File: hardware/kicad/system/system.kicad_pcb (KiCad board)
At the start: 2 copper layers, 203 x 133 mm, 131 parts, among them M501 IRF530, Q201 IRF540N, Q202 IRF530, Q401 IRF530, SW201 Switch, U201 LM7805, U202 MCP601, U203 NE555, U204 ILD74, U205 MCP601, U206 IR2110, U207 4N25, U208 IR2110, U301 MCP601, U302 IL300, U303 MCP601, U401 CNY17, U402 IR2110, U501 CNY17, U502 IR2110

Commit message: system PCB: scripted placement recovery (auto-floorplan)
Rebuild the integrated-board placement after an unsaved-work loss, via
tools/place_system.py (pcbnew): edge connectors on the borders, the 5 board
clusters shelf-packed into their regions (big parts first), test-point row
along the bottom, R_STAR on the GND/GND_MCU boundary, Edge.Cuts 200x130 mm
(<=203.2 wide for the SRM-20). All 131 footprints on-board, non-overlapping.
First-pass auto-placement; fine-tune by hand from here.
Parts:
- moved U301 336.7 mm to (23.5, 105.5)
- moved R302 336.4 mm to (23.1, 118.7)
- moved U302 335.2 mm to (36.5, 105.5)
- moved U303 333.7 mm to (49.6, 105.5)
- moved R305 323.0 mm to (35.3, 118.7)
- moved R301 312.6 mm to (47.6, 118.7)
- moved Q401 312.4 mm to (111.7, 75.0)
- moved R403 311.4 mm to (99.1, 83.8)
- moved C404 309.7 mm to (100.7, 75.8)
- moved D403 300.2 mm to (123.0, 83.6)
- moved R401 297.1 mm to (111.0, 83.8)
- moved U402 296.9 mm to (136.7, 25.6)
- moved R303 295.7 mm to (62.3, 105.5)
- moved R402 293.4 mm to (122.8, 73.1)
- moved L401 290.6 mm to (101.4, 41.3)
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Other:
- board size 203 x 133 mm -> 200 x 130 mm

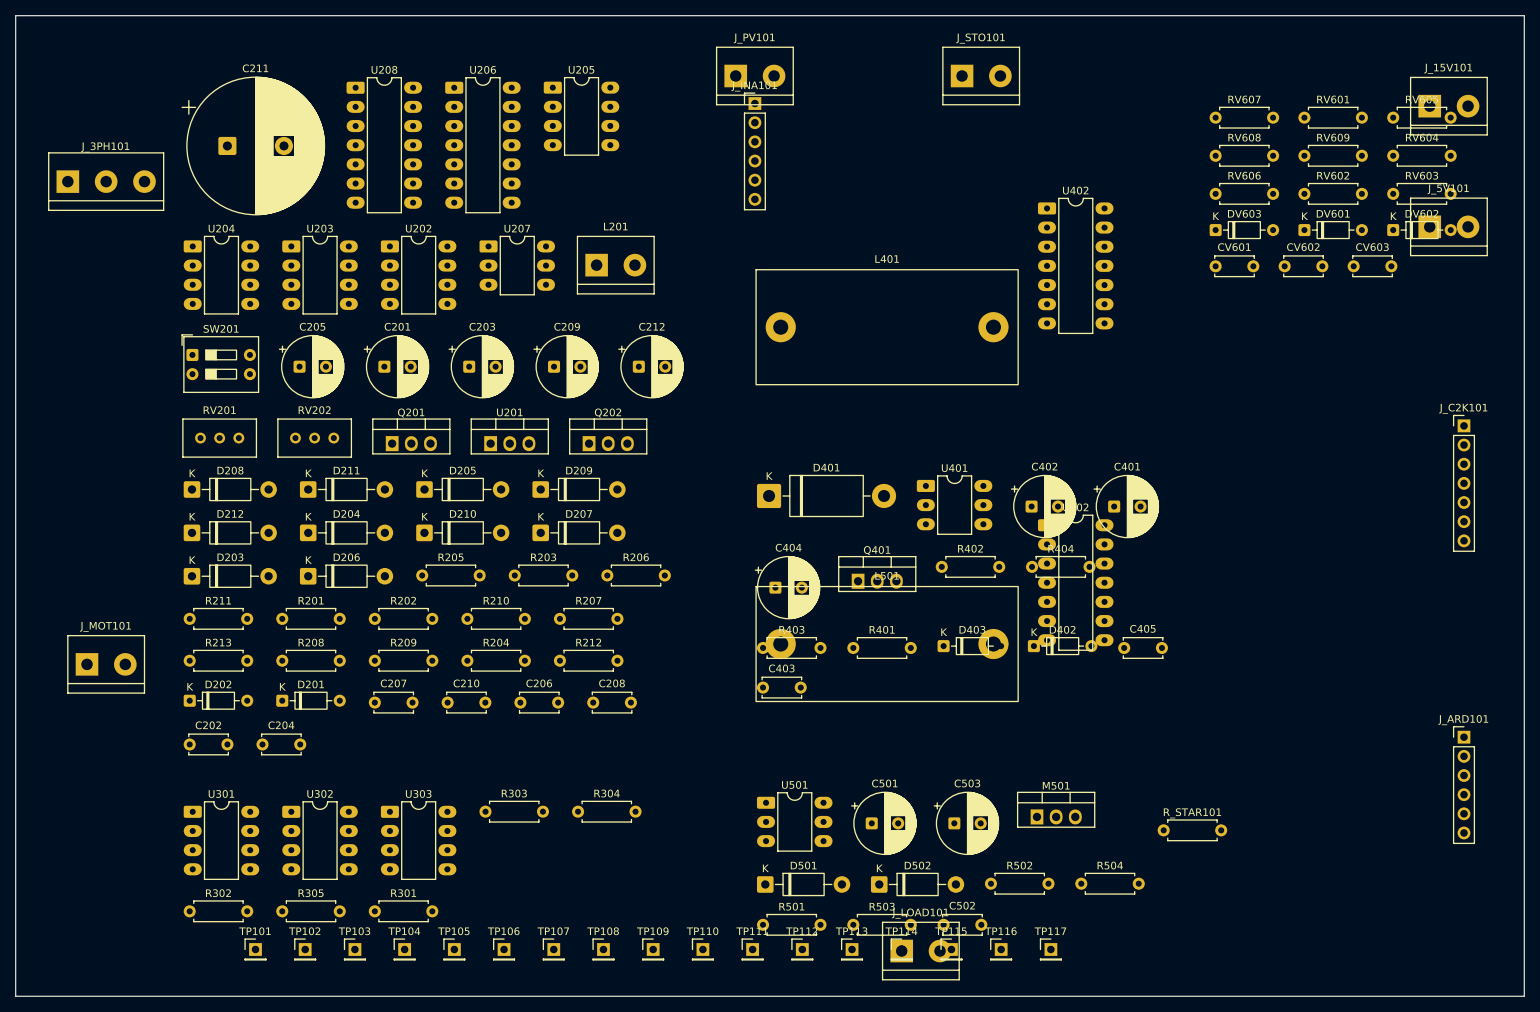
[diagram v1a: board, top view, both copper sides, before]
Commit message: system PCB: repack placement — 0 overlaps, toroids fixed, clusters clear
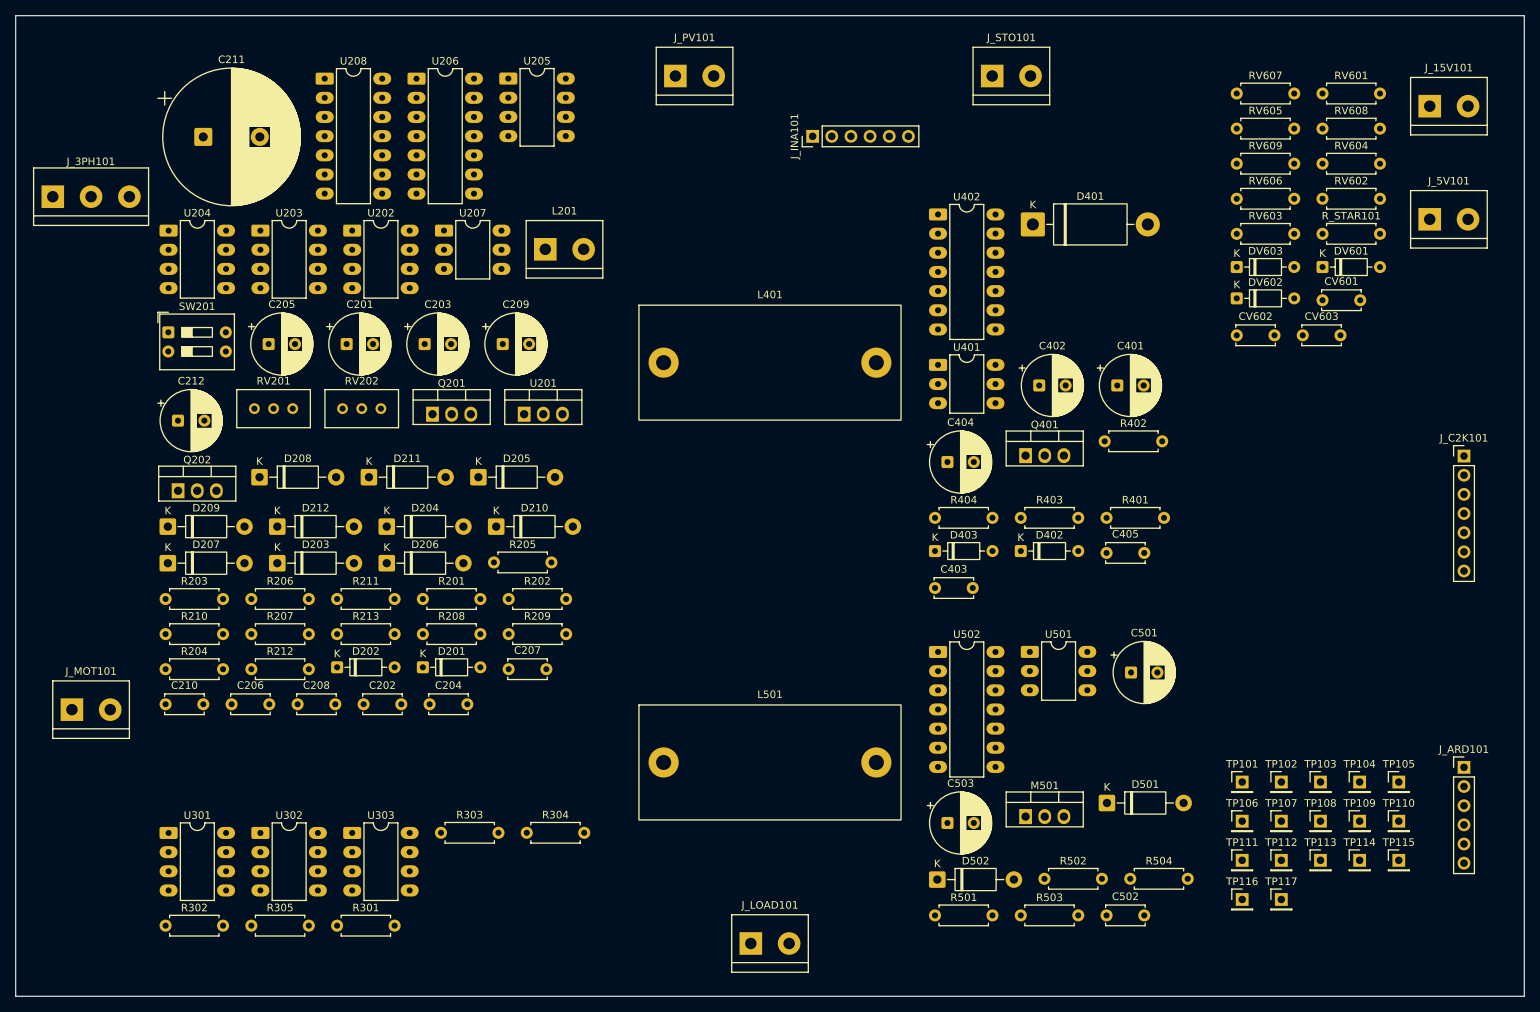
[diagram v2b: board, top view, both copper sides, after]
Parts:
- moved TP101 132.7 mm to (162.6, 101.6)
- moved TP102 131.3 mm to (167.8, 101.6)
- moved TP103 129.9 mm to (173.0, 101.6)
- moved TP104 128.5 mm to (178.2, 101.6)
- moved TP105 127.2 mm to (183.4, 101.6)
- moved TP106 99.3 mm to (162.6, 106.8)
- moved TP107 97.9 mm to (167.8, 106.8)
- moved TP108 96.6 mm to (173.0, 106.8)
- moved TP109 95.2 mm to (178.2, 106.8)
- moved TP110 93.8 mm to (183.4, 106.8)
- moved R_STAR101 81.8 mm to (173.2, 28.9)
- moved TP111 66.0 mm to (162.6, 112.0)
- moved TP112 64.6 mm to (167.8, 112.0)
- moved TP113 63.2 mm to (173.0, 112.0)
- moved TP114 61.8 mm to (178.2, 112.0)
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
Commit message: system PCB: routing prep (track 1.0, GND pour both layers) + board/CAM updates
system board:
- fix Default netclass track 0.9 -> 1.0 mm (was below min_track_width, every
  trace would have failed DRC); clearance 1.0, via 2.4/1.0 in .kicad_pro + board
- pour GND on F.Cu and B.Cu (edge inset 0.5 mm, solid pad tie)
- routing tooling: route_prep (netclass+pour), export_dsn_noplane (route GND as
  tracks; Freerouting 1.9.0 chokes on full-board planes), route_finish (SES
  import + refill + sparse GND stitching), inspect_system

srm-cam: bump submodule to double-sided support (90 rotation, bottom-side bed
leveling, GUI ruler/STOP/probe-grid, run-time estimator)

production: rename boost_v2_mill nc -> board_*, add drive_circuit trace rework
boards: buck_v2, current_sense, c2000_feedback edits; BOM + AD3 lab-guide
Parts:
- moved J_5V101 126.8 mm to (290.6, 100.7), turned to 90 degrees
- moved J_LOAD101 126.2 mm to (198.0, 199.2), turned to 180 degrees
- moved J_15V101 124.3 mm to (290.5, 81.6), turned to -90 degrees
- moved J_3PH101 122.0 mm to (99.1, 101.6), turned to 90 degrees
- moved J_PV101 119.8 mm to (185.4, 77.0)
- moved C209 119.6 mm to (159.2, 116.7)
- moved C203 119.6 mm to (148.9, 116.7)
- moved C401 119.6 mm to (240.7, 122.2)
- moved C201 119.6 mm to (138.5, 116.7)
- moved C402 119.6 mm to (230.3, 122.2)
- moved M501 119.6 mm to (228.5, 179.4)
- moved Q401 119.6 mm to (228.5, 131.5)
- moved C501 119.6 mm to (242.5, 160.3)
- moved C205 119.6 mm to (128.2, 116.7)
- moved R402 119.6 mm to (239.0, 129.6)
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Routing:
- net +5V_PWR: track 0.00 -> 553.1 mm, vias 0 -> 2
- net GND_MCU: track 0.00 -> 334.7 mm, vias 0 -> 4
- net +15V2: track 0.00 -> 313.8 mm, vias 0 -> 3
- net V1: track 0.00 -> 309.6 mm, vias 0 -> 2
- net +15V_GATE: track 0.00 -> 285.4 mm
- net PV_SDA: track 0.00 -> 256.6 mm, vias 0 -> 1
- net STORE: track 0.00 -> 252.2 mm
- net PWM_MOTOR: track 0.00 -> 220.0 mm, vias 0 -> 1
- net 3PH_W: track 0.00 -> 216.7 mm, vias 0 -> 4
- net 3PH_U: track 0.00 -> 193.7 mm, vias 0 -> 3
- net PV_SCL: track 0.00 -> 178.8 mm, vias 0 -> 3
- net Net-(U203-THRES): track 0.00 -> 175.0 mm, vias 0 -> 4
- net LOAD: track 0.00 -> 166.8 mm, vias 0 -> 1
- net MCU_V1: track 0.00 -> 165.7 mm
- net ADC_V1: track 0.00 -> 161.6 mm
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- added copper zone on B.Cu, net GND
- added copper zone on F.Cu, net GND

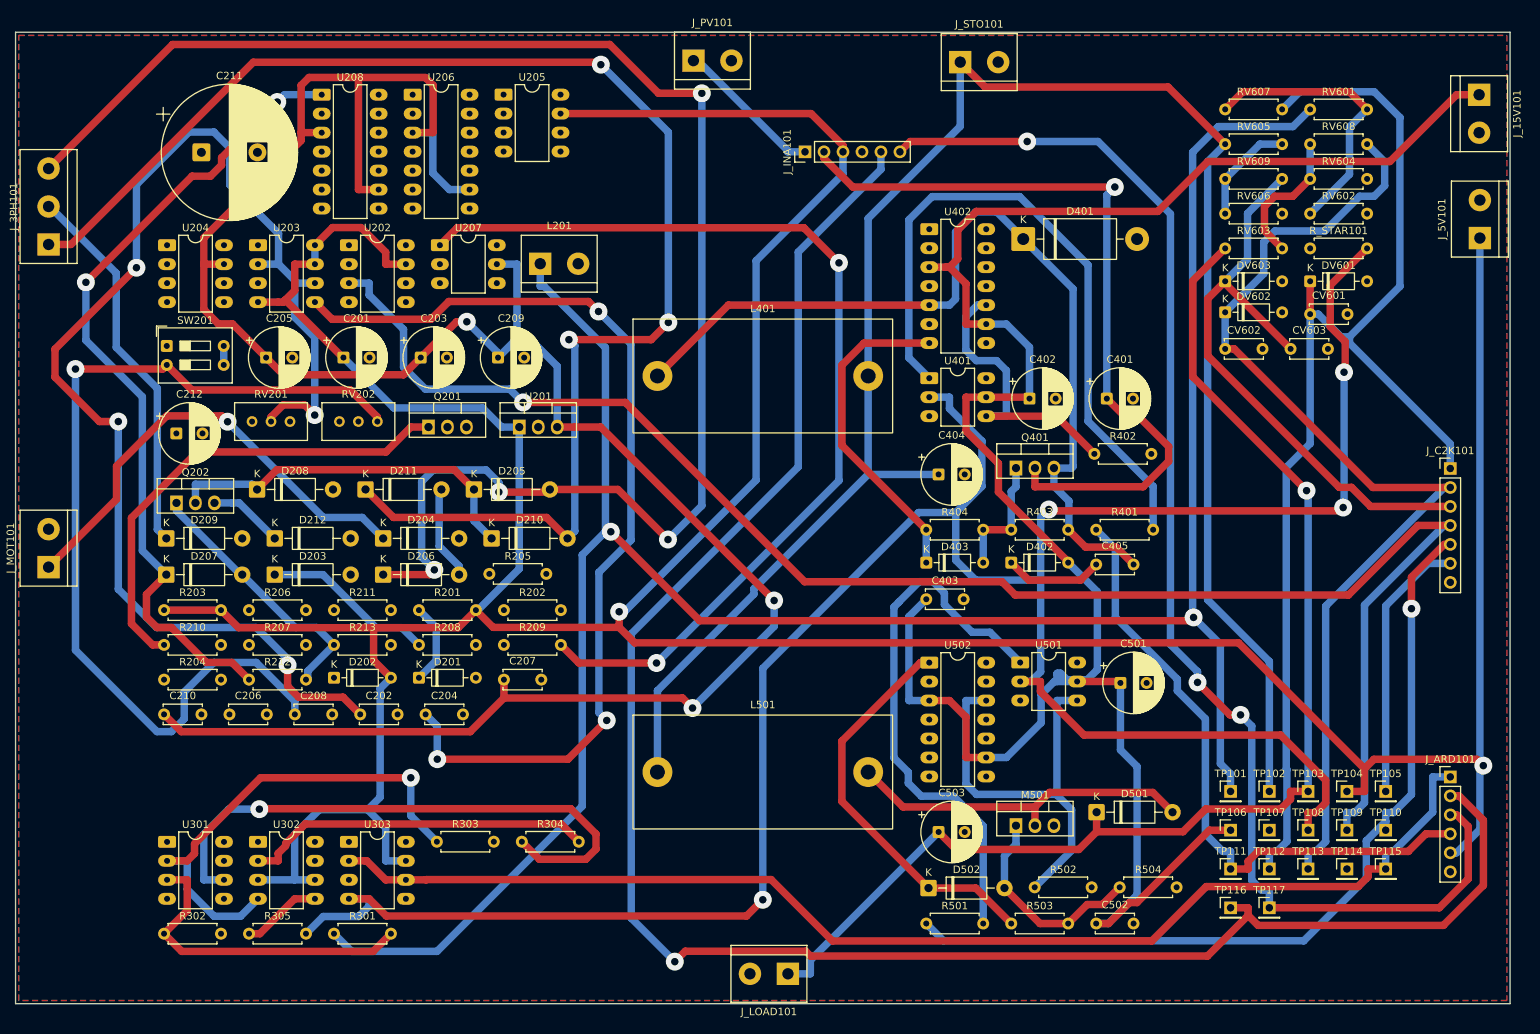
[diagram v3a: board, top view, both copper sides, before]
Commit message: system PCB: route both layers (Freerouting), DRC-clean, millable
- 1199 tracks + 67 vias (61 signal from the router + 6 GND stitches); every
  real net routed at 1.0 mm clearance, GND poured both layers
- custom DRU: pad-to-pad floor 0.8 mm (fixed 2.54 mm THT pitch can't reach the
  1.0 mm routed-copper rule) -> DRC clearance violations 246 -> 0
- gerber2rml preflight: 0.4 mm bit 0 un-millable gaps; 0.8 mm bit only 2 (0.38 mm2)
- remaining DRC: 4 silk-over-edge (cosmetic) + 24 netless NC/unused pins (benign)
- system_routed.pdf: F.Cu/B.Cu/Edge.Cuts for review
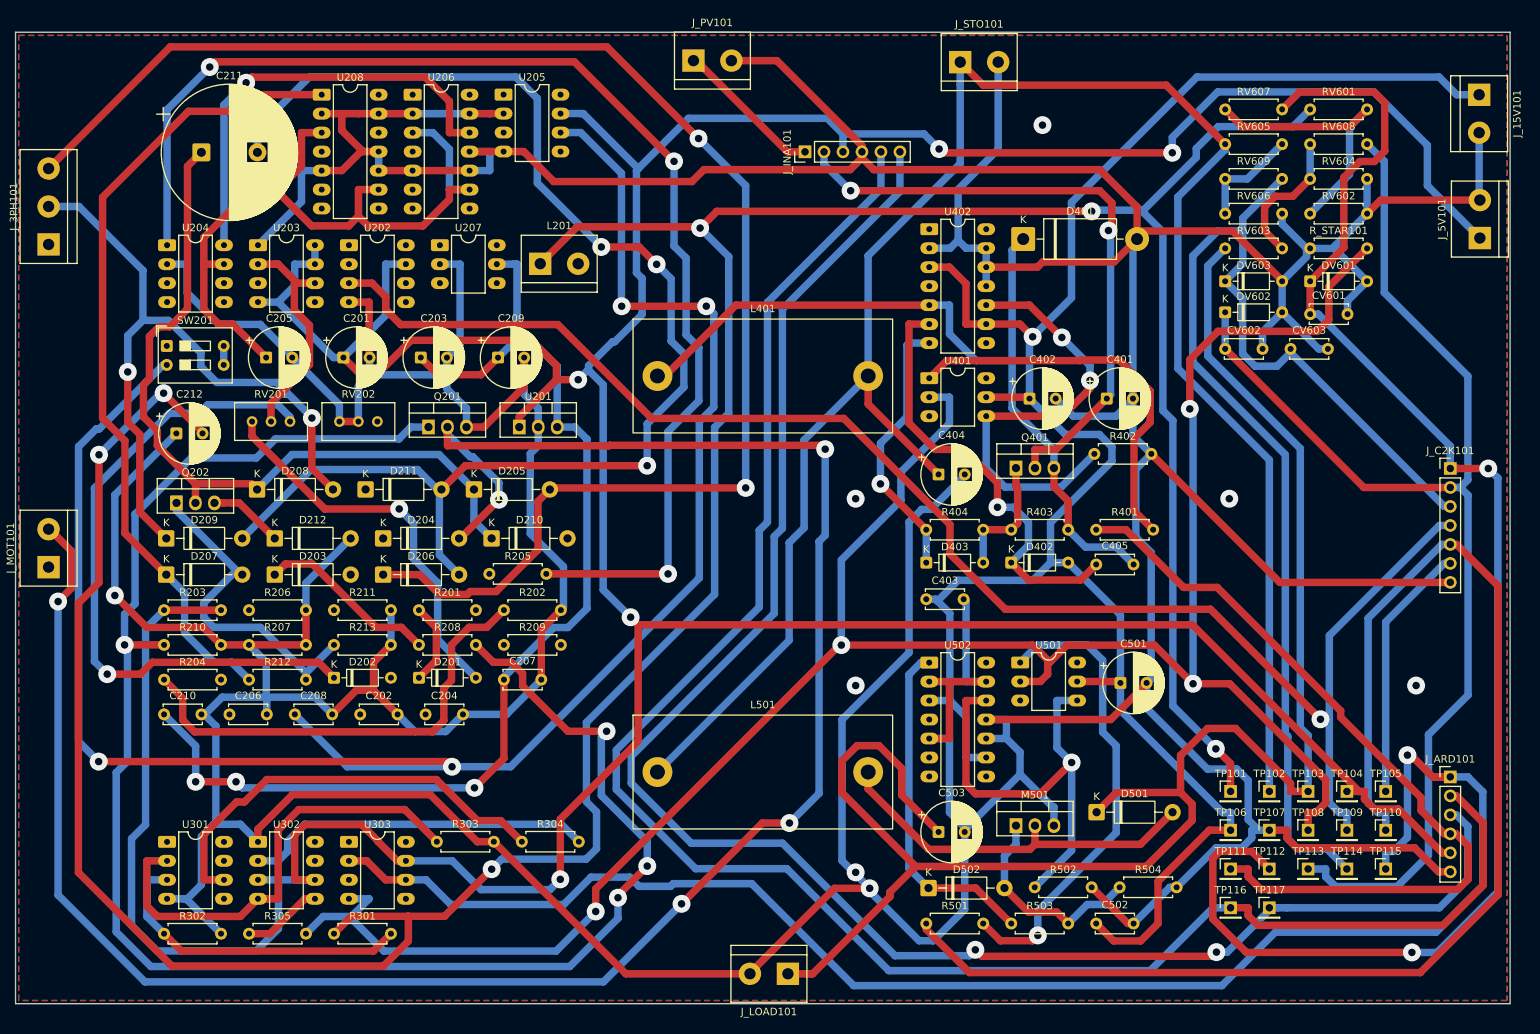
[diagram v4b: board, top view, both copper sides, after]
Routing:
- net GND: track 0.00 -> 1215.0 mm, vias 0 -> 8
- net MOTOR_B: track 0.00 -> 288.1 mm, vias 0 -> 5
- net 3PH_U: track 193.7 -> 0.00 mm, vias 3 -> 0
- net Net-(R205-Pad2): track 0.00 -> 168.7 mm, vias 0 -> 3
- net Net-(D206-A): track 12.6 -> 179.8 mm, vias 0 -> 3
- net Net-(D203-A): track 64.5 -> 231.1 mm, vias 0 -> 4
- net V1: track 309.6 -> 458.7 mm, vias 2 -> 6
- net Net-(U203-THRES): track 175.0 -> 30.4 mm, vias 4 -> 0
- net Net-(R209-Pad2): track 133.8 -> 0.00 mm, vias 2 -> 0
- net Net-(U203-CONT): track 130.7 -> 0.00 mm, vias 3 -> 0
- net Net-(C208-Pad1): track 125.5 -> 251.8 mm, vias 1 -> 4
- net Net-(D202-K): track 0.00 -> 89.5 mm, vias 0 -> 1
- net ADC_STORE: track 81.3 -> 166.7 mm
- net PWM_BOOST: track 114.9 -> 179.1 mm, vias 1 -> 0
- net +15V2: track 313.8 -> 250.0 mm
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
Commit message: system PCB: narrow THT pads for 0.8 mm bit + connectivity-aware re-placement
- narrow_pads.py: clamp the close-neighbour pad dimension to 1.40 mm on dense
  (<=2.54 mm-pitch) parts -> inter-pin gaps 0.84/0.94 -> 1.14 mm. Clears the
  1.0 mm clearance rule outright and gives a 0.8 mm end mill 0.34 mm margin
  (168 pads / 23 parts: DIPs, optos, TO-220s, 2.54 mm headers, DIP switch)
- place_system2.py: force-directed per-region placement, related parts cluster
  (decoupling by IC, gate parts by MOSFET, divider Rs by op-amp), pulled toward
  each region's fixed connectors/toroids; 0.5 mm grid snap, shelf fallback,
  0 overlaps. Routing must be stripped first (strip_all_routing.py, textual --
  in-process pcbnew Remove() corrupts SWIG iterators)
- old routing stripped; board is placed + unrouted, ready to re-route
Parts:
- moved C207 183.4 mm to (30.0, 30.5)
- moved D201 168.0 mm to (50.2, 23.5)
- moved C210 166.5 mm to (50.0, 11.0)
- moved U201 161.3 mm to (28.0, 36.5)
- moved R209 159.5 mm to (51.2, 38.5)
- moved D202 156.7 mm to (25.2, 50.0)
- moved R211 154.9 mm to (38.7, 31.0)
- moved D212 153.9 mm to (25.9, 27.0)
- moved C405 153.7 mm to (122.0, 45.0)
- moved L201 153.5 mm to (40.0, 15.0)
- moved R202 152.3 mm to (52.7, 42.5)
- moved C206 148.8 mm to (41.0, 40.5)
- moved C204 147.5 mm to (43.0, 62.5)
- moved R201 145.2 mm to (60.7, 35.0)
- moved D204 144.4 mm to (36.4, 44.5)
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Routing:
- net GND: track 1215.0 -> 0.00 mm, vias 8 -> 0
- net +5V_PWR: track 606.6 -> 0.00 mm, vias 5 -> 0
- net V1: track 458.7 -> 0.00 mm, vias 6 -> 0
- net GND_MCU: track 305.7 -> 0.00 mm, vias 4 -> 0
- net MOTOR_B: track 288.1 -> 0.00 mm, vias 5 -> 0
- net +15V_GATE: track 279.2 -> 0.00 mm, vias 1 -> 0
- net STORE: track 263.2 -> 0.00 mm
- net Net-(C208-Pad1): track 251.8 -> 0.00 mm, vias 4 -> 0
- net +15V2: track 250.0 -> 0.00 mm, vias 3 -> 0
- net PV_SDA: track 247.6 -> 0.00 mm
- net PV_SCL: track 236.2 -> 0.00 mm, vias 2 -> 0
- net Net-(D203-A): track 231.1 -> 0.00 mm, vias 4 -> 0
- net LOAD: track 225.4 -> 0.00 mm
- net MCU_V1: track 211.6 -> 0.00 mm, vias 1 -> 0
- net PWM_MOTOR: track 208.6 -> 0.00 mm, vias 1 -> 0
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- removed copper zone on B.Cu, net GND
- removed copper zone on F.Cu, net GND
